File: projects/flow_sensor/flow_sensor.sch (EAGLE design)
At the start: 64 parts, among them IC1 TPS61201, IC5 REG1118

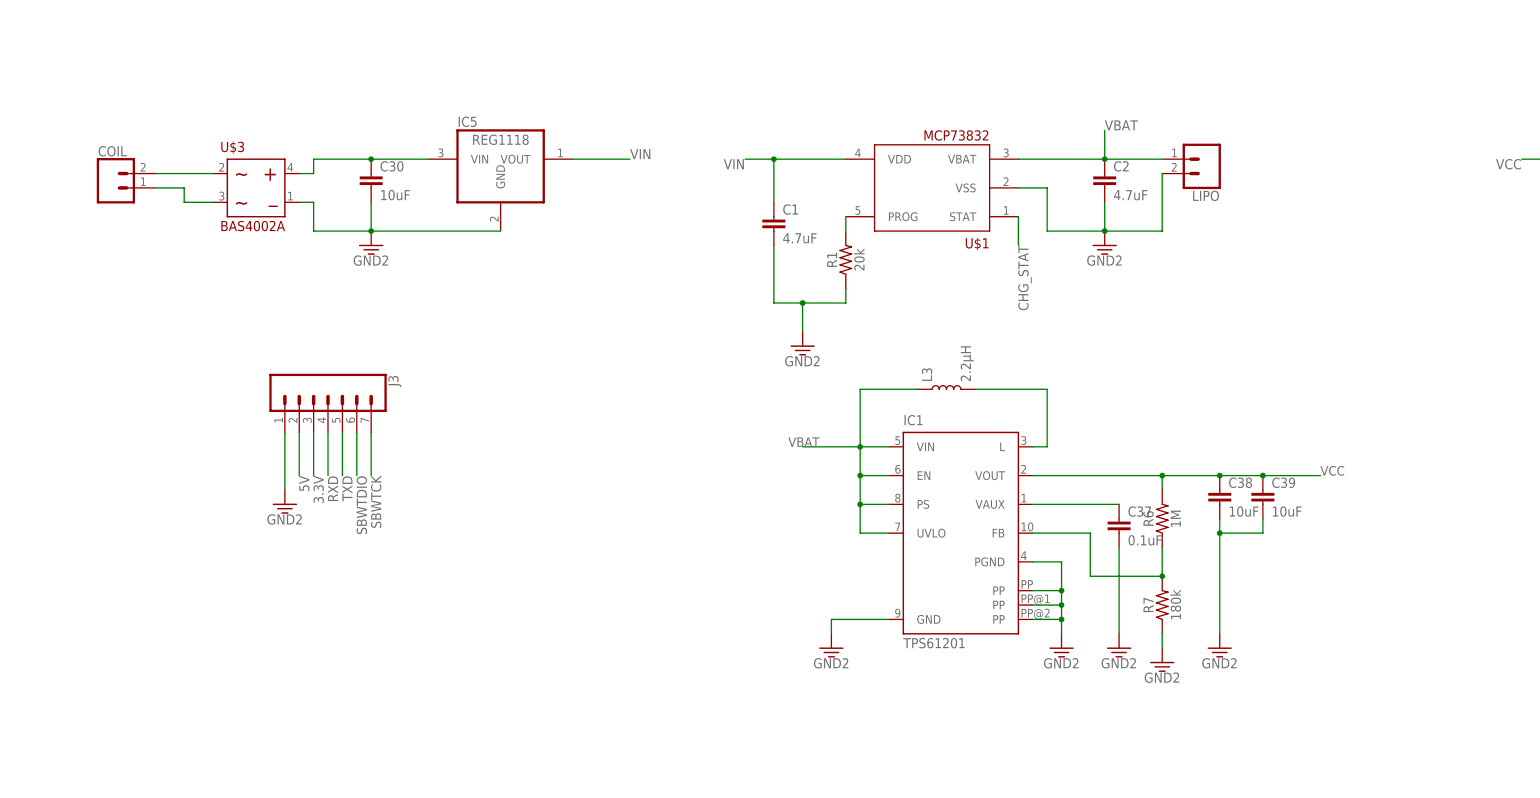
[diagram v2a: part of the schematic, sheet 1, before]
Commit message: Modified power supply to run off of NFC chip supply
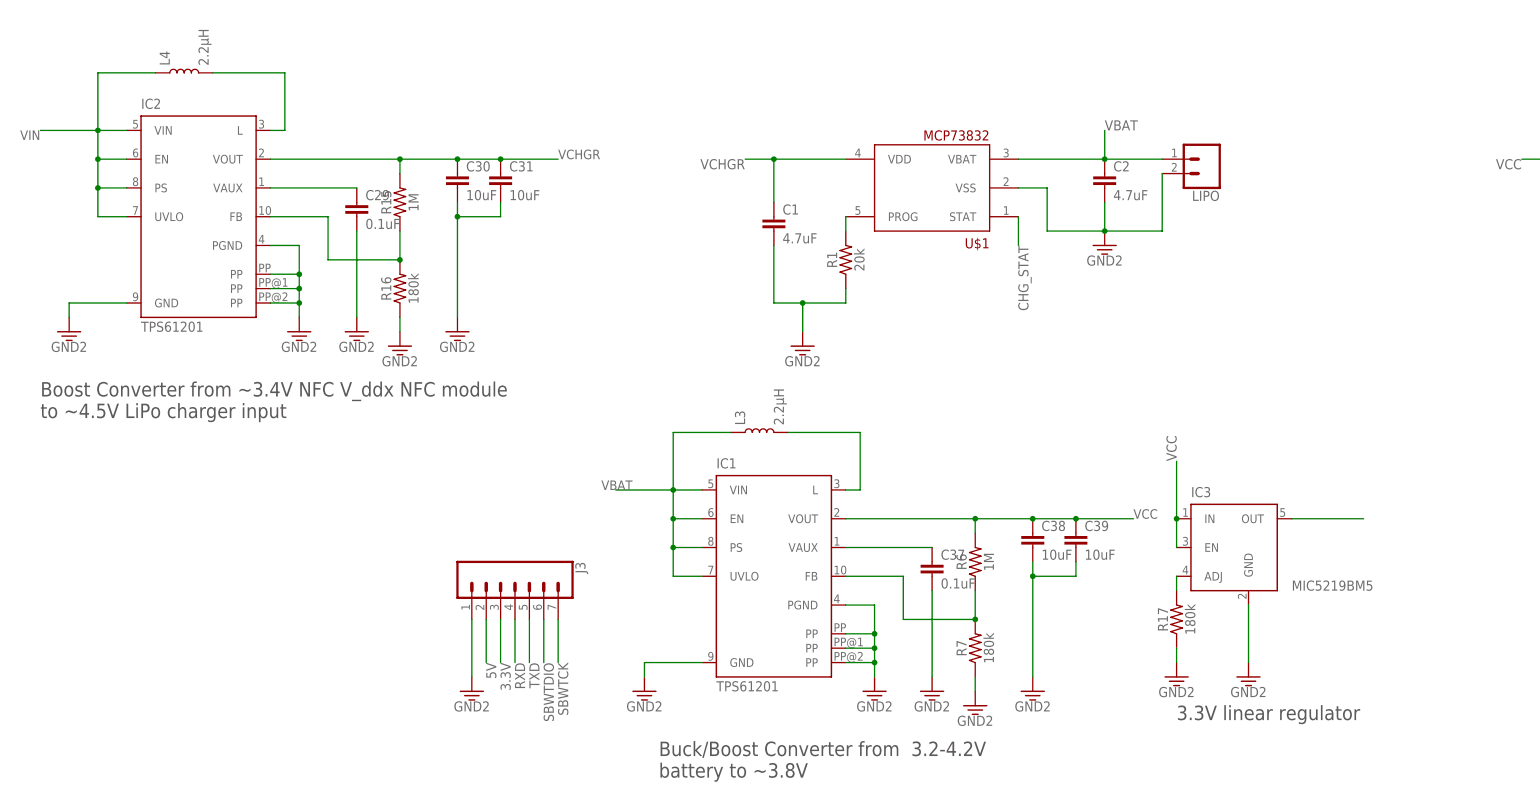
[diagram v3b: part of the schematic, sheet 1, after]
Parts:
- removed COIL: (no value), SparkFun-Connectors:CONN_021X02_NO_SILK
- removed IC5: REG1118, burr-brown:REG1118
- removed U$3: BAS4002A, my_library:BAS4002A
- added C29: 0.1uF, SparkFun-Capacitors:0.1UF-0603-25V-(+80/-20%)
- added C31: 10uF, SparkFun-Capacitors:10UF-0603-6.3V-20%
- added IC2: TPS61201, texas:TPS61201
- added IC3: MIC5219BM5, v-reg-micrel:MIC5219BM5
- added L4: 2.2µH, SparkFun-Coils:INDUCTOR-0805-3.3UH
- added R15: 1M, SparkFun-Resistors:1MOHM-0603-1/4W-5%
- added R16, R17: 180k, SparkFun-Resistors:180OHM-0603-1/10W-1%
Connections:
- removed net POWERCOIL: COIL.2, U$3.~
- removed net POWERCOIL': COIL.1, U$3.~'
- removed net UNREG+: C30.1, IC5.VIN, U$3.+
- new net N$1: IC2.L, L4.2
- new net N$18: C29.1, IC2.VAUX
- new net N$22: IC2.FB, R15.1, R16.2
- new net N$25: IC3.ADJ, R17.2
- new net VCHGR: C1.1, C30.1, C31.1, C5.1, C6.1, IC2.VOUT, R15.2, U$1.VDD, U$2.VIN
- net 3.3V: now also IC3.GND, R17.1
- net GND: now also C29.2, C31.2, IC2.GND, IC2.PGND, IC2.PP, IC2.PP@1, IC2.PP@2, R16.1; no longer IC5.GND, U$3.-
- net N$6: now also IC3.OUT; no longer C7.1, C8.1, R4.1, R5.1, U$2.VDD_I/O, U$2.VDD_X
- net VCC: now also IC3.EN, IC3.IN; no longer C5.1, C6.1, U$2.VIN
- net VIN: now also C7.1, C8.1, IC2.EN, IC2.PS, IC2.UVLO, IC2.VIN, L4.1, R4.1, R5.1, U$2.VDD_I/O, U$2.VDD_X; no longer C1.1, IC5.VOUT, U$1.VDD
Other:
- note added: "3.3V linear regulator"
- note added: "Boost Converter from ~3.4V NFC V_ddx NFC module to ~4.5V LiPo charger input"
- note added: "Buck/Boost Converter from 3.2-4.2V battery to ~3.8V"
- moved on the sheet: C30, C37, C38, C39, IC1, J3, L3, R6, R7

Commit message: Board created, general save dump
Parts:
- added C32, C33: 0.1uF, SparkFun-Capacitors:0.1UF-0603-25V-(+80/-20%)
- added C34, C36: 68.0pF, SparkFun-Capacitors:1.0PF-0603-50V-25%
- added C35, C42: 1.0pF, SparkFun-Capacitors:1.0PF-0603-50V-25%
- added J1, J2: (no value), SparkFun-Connectors:CONN_02
- added R18: 680, SparkFun-Resistors:680OHM-0603-1/10W-5%
- C1: value 4.7uF -> 0.1uF; device SparkFun-Capacitors:4.7UF0603 -> SparkFun-Capacitors:0.1UF-0603-25V-(+80/-20%)
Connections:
- removed net 3.3V: IC3.GND, J3.3, R17.1, U$5.VCC-
- removed net N$6: IC3.OUT
- new net IRQ: U$2.IRQ
- new net N$27: C34.1, C35.1, J1.2
- new net N$30: C38.1, C39.1, IC1.VOUT, IC3.EN, IC3.IN, R6.2
- net ANT: now also J1.1
- net GND: now also C1.1, C32.1, C33.1, C34.2, C35.2, C36.1, C36.2, C42.1, C42.2, IC3.GND, J2.1, J2.2, J3.3, R17.1, R18.1, R18.2, U$5.VCC-; no longer C1.2
- net N$12: now also C15.1, C18.2
- net N$15: now also C15.2, C18.1
- net VCC: now also C1.2, C32.2, C33.2, C5.1, C6.1, IC3.OUT, U$2.VIN; no longer C38.1, C39.1, IC1.VOUT, IC3.EN, IC3.IN, R6.2
- net VCHGR: no longer C1.1, C5.1, C6.1, U$2.VIN
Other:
- moved on the sheet: C1

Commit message: Second data dump.  Board Layout Complete
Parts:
- added C43: 0.1uF, SparkFun-Capacitors:0.1UF-0603-25V-(+80/-20%)
- added C44: 2.2n, SparkFun-Capacitors:1.0UF-0603-16V-10%
- added D1, D2, D3: (no value), SparkFun-LED:LED0603
- added J5: 455-1750-1-ND, SparkFun-Connectors:CONN_03
- added R19, R20: 10k, SparkFun-Resistors:10KOHM-0603-1/10W-1%
- added R21, R22, R23: 680, SparkFun-Resistors:680OHM-0603-1/10W-5%
- added R24: 47k, SparkFun-Resistors:680OHM-0603-1/10W-5%
- added U$6: ADT7320, my_library:ADT7320
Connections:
- removed net CLK: U$2.DATA_CLK, U$9.(UCA0CLK/A5)P1.5
- removed net SIMO: U$2.I/O_7, U$9.(UCA0TXD/UCA0SIMO)P2.0
- removed net SOMI: U$2.I/O_6, U$9.(UCA0RXD/UCA0SOMI)P2.1
- removed net STE: U$9.(UCA0STE/A4)P1.4
- new net 3V3: J3.3
- new net MISO: U$2.I/O_6, U$6.MISO, U$9.(UCB0SCL/UCB0SOMI)P1.7
- new net MOSI: U$2.I/O_7, U$6.MOSI, U$9.(UCB0SDA/UCB0SIMO)P1.6
- new net N$26: R20.2, U$6.CT
- new net N$31: D3.A, R23.1
- new net N$32: D2.A, R22.1
- new net N$33: D1.A, R21.1
- new net N$34: R21.2, U$9.(A8)P4.0
- new net N$35: R22.2, U$9.(A9)P4.1
- new net N$38: R23.2, U$9.(A10)P4.2
- new net N$6: R19.2, U$6.INT
- new net SCLK: U$2.DATA_CLK, U$6.SCLK, U$9.(UCB0CLK)P2.2
- new net TEMP_SS: U$6.CS, U$9.P4.6
- net 5V: now also J5.2
- net CHG_STAT: now also U$9.P3.4
- net COM_EN: now also U$9.P3.5
- net COM_EN2: now also U$9.P3.6
- net COM_SS: now also U$9.P4.5
- net GND: now also C43.2, C44.1, D1.C, D2.C, D3.C, U$6.GND; no longer J3.3
- net IRQ: now also U$9.P3.7
- net N$30: now also J5.1
- net RXD: now also U$9.(UCA0RXD/UCA0SOMI)P2.1
- net SBWTDIO: now also C44.2, R24.1
- net SENSOR_OUT: now also U$9.(A2)P1.2
- net TXD: now also U$9.(UCA0TXD/UCA0SIMO)P2.0
- net VCC: now also C43.1, R19.1, R20.1, R24.2, U$6.VDD
- net VCHGR: now also J5.3
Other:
- moved on the sheet: C19

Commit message: Touched up board V1.0, added labels
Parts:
- IC1, IC2: value TPS61201 -> TPS61200; device texas:TPS61201 -> texas:TPS61200
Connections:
- net COM_EN renamed COMMS_EN
- net COM_EN2 renamed COMMS_EN2
- net COM_SS renamed COMMS_SS
- net IRQ renamed COMMS_IRQ
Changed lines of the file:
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@@
 <part name="C23" library="SparkFun-Capacitors" deviceset="100PF" device="-0603-50V-5%" value="100pF"/>
 <part name="C24" library="SparkFun-Capacitors" deviceset="27PF" device="-0603-50V-5%" value="27pF"/>
-<part name="IC1" library="texas" library_urn="urn:adsk.eagle:library:387" deviceset="TPS6120*" device="" technology="1"/>
+<part name="IC1" library="texas" library_urn="urn:adsk.eagle:library:387" deviceset="TPS6120*" device="" technology="0" value="TPS61200"/>
 <part name="L3" library="SparkFun-Coils" deviceset="INDUCTOR" device="-0805-3.3UH" value="2.2µH"/>
 <part name="R6" library="SparkFun-Resistors" deviceset="1MOHM" device="-0603-1/4W-5%" value="1M"/>
@@
 <part name="R11" library="SparkFun-Resistors" deviceset="1.5KOHM" device="-0603-1/10W-1%" value="1.5k"/>
 <part name="R12" library="SparkFun-Resistors" deviceset="8.2KOHM" device="-0603-1/10W-5%" value="1.5k"/>
-<part name="IC2" library="texas" library_urn="urn:adsk.eagle:library:387" deviceset="TPS6120*" device="" technology="1"/>
+<part name="IC2" library="texas" library_urn="urn:adsk.eagle:library:387" deviceset="TPS6120*" device="" technology="0" value="TPS61200"/>
 <part name="L4" library="SparkFun-Coils" deviceset="INDUCTOR" device="-0805-3.3UH" value="2.2µH"/>
 <part name="R15" library="SparkFun-Resistors" deviceset="1MOHM" device="-0603-1/4W-5%" value="1M"/>
@@
 </segment>
 </net>
-<net name="COM_EN" class="0">
+<net name="COMMS_EN" class="0">
 <segment>
 <pinref part="U$2" gate="G$1" pin="EN"/>
@@
 </segment>
 </net>
-<net name="COM_EN2" class="0">
+<net name="COMMS_EN2" class="0">
 <segment>
 <pinref part="U$2" gate="G$1" pin="EN2"/>
@@
 </segment>
 </net>
-<net name="COM_SS" class="0">
+<net name="COMMS_SS" class="0">
 <segment>
 <pinref part="U$2" gate="G$1" pin="I/O_4"/>
@@
 </segment>
 </net>
-<net name="IRQ" class="0">
+<net name="COMMS_IRQ" class="0">
 <segment>
 <pinref part="U$2" gate="G$1" pin="IRQ"/>

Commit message: starting v2.0
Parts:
- removed R11, R14: 1.5k, SparkFun-Resistors:1.5KOHM-0603-1/10W-1%
- removed R12, R13: 1.5k, SparkFun-Resistors:8.2KOHM-0603-1/10W-5%
- added J4: (no value), SparkFun-Connectors:CONN_021X02_NO_SILK
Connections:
- net GND: no longer R13.2, R14.2
- net N$28: now also J4.2; no longer R11.2, R14.1
- net N$29: now also J4.1; no longer R12.2, R13.1
- net VCC: no longer R11.1, R12.1
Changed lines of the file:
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@@
 <part name="R9" library="SparkFun-Resistors" deviceset="10KOHM" device="-0603-1/10W-1%" value="10k"/>
 <part name="R10" library="SparkFun-Resistors" deviceset="787OHM" device="-0603-1/10W-1%" value="600"/>
-<part name="R13" library="SparkFun-Resistors" deviceset="8.2KOHM" device="-0603-1/10W-5%" value="1.5k"/>
-<part name="R14" library="SparkFun-Resistors" deviceset="1.5KOHM" device="-0603-1/10W-1%" value="1.5k"/>
-<part name="GND24" library="SparkFun-PowerSymbols" deviceset="GND2" device=""/>
 <part name="C28" library="SparkFun-Capacitors" deviceset="4.7UF" device="0603" value="3uF"/>
 <part name="U$4" library="my_library" deviceset="AD8222" device=""/>
@@
 <part name="C41" library="SparkFun-Capacitors" deviceset="4.7UF" device="0603" value="3uF"/>
 <part name="U$5" library="my_library" deviceset="LM321" device=""/>
-<part name="R11" library="SparkFun-Resistors" deviceset="1.5KOHM" device="-0603-1/10W-1%" value="1.5k"/>
-<part name="R12" library="SparkFun-Resistors" deviceset="8.2KOHM" device="-0603-1/10W-5%" value="1.5k"/>
 <part name="IC2" library="texas" library_urn="urn:adsk.eagle:library:387" deviceset="TPS6120*" device="" technology="0" value="TPS61200"/>
 <part name="L4" library="SparkFun-Coils" deviceset="INDUCTOR" device="-0805-3.3UH" value="2.2µH"/>
@@
 <part name="C44" library="SparkFun-Capacitors" deviceset="1.0UF" device="-0603-16V-10%" value="2.2n"/>
 <part name="GND42" library="SparkFun-PowerSymbols" deviceset="GND" device=""/>
+<part name="J4" library="SparkFun-Connectors" deviceset="CONN_02" device="1X02_NO_SILK"/>
 </parts>
 <sheets>
@@
 <instance part="R9" gate="G$1" x="261.62" y="53.34"/>
 <instance part="R10" gate="G$1" x="215.9" y="17.78"/>
-<instance part="R13" gate="G$1" x="180.34" y="55.88"/>
-<instance part="R14" gate="G$1" x="180.34" y="68.58"/>
-<instance part="GND24" gate="G$1" x="190.5" y="63.5" rot="R90"/>
 <instance part="C28" gate="G$1" x="271.78" y="58.42" rot="R90"/>
 <instance part="U$4" gate="G$1" x="215.9" y="43.18"/>
@@
 <instance part="C41" gate="G$1" x="271.78" y="45.72" rot="R270"/>
 <instance part="U$5" gate="G$1" x="304.8" y="50.8"/>
-<instance part="R11" gate="G$1" x="165.1" y="68.58"/>
-<instance part="R12" gate="G$1" x="165.1" y="55.88"/>
 <instance part="IC2" gate="G$1" x="-83.82" y="53.34"/>
 <instance part="L4" gate="G$1" x="-86.36" y="78.74" rot="R90"/>
@@
 <instance part="GND40" gate="1" x="208.28" y="-7.62" rot="R180"/>
 <instance part="J5" gate="J$1" x="55.88" y="17.78"/>
+<instance part="J4" gate="G$1" x="177.8" y="50.8"/>
 </instances>
 <busses>
@@
 <junction x="228.6" y="40.64"/>
 <pinref part="GND21" gate="1" pin="GND"/>
-</segment>
-<segment>
-<pinref part="R13" gate="G$1" pin="2"/>
-<pinref part="R14" gate="G$1" pin="2"/>
-<wire x1="185.42" y1="55.88" x2="185.42" y2="63.5" width="0.1524" layer="91"/>
-<wire x1="185.42" y1="63.5" x2="185.42" y2="68.58" width="0.1524" layer="91"/>
-<wire x1="185.42" y1="63.5" x2="187.96" y2="63.5" width="0.1524" layer="91"/>
-<junction x="185.42" y="63.5"/>
-<pinref part="GND24" gate="G$1" pin="3.3V"/>
 </segment>
 <segment>
@@
 </segment>
 <segment>
-<wire x1="160.02" y1="55.88" x2="160.02" y2="63.5" width="0.1524" layer="91"/>
-<wire x1="160.02" y1="63.5" x2="160.02" y2="68.58" width="0.1524" layer="91"/>
-<wire x1="160.02" y1="63.5" x2="149.86" y2="63.5" width="0.1524" layer="91"/>
-<junction x="160.02" y="63.5"/>
-<label x="149.86" y="63.5" size="1.778" layer="95" rot="R180"/>
-<pinref part="R11" gate="G$1" pin="1"/>
-<pinref part="R12" gate="G$1" pin="1"/>
-</segment>
-<segment>
 <wire x1="309.88" y1="60.96" x2="309.88" y2="66.04" width="0.1524" layer="91"/>
 <pinref part="U$5" gate="G$1" pin="VCC+"/>
@@
 <net name="N$28" class="0">
 <segment>
-<pinref part="R14" gate="G$1" pin="1"/>
-<wire x1="170.18" y1="68.58" x2="172.72" y2="68.58" width="0.1524" layer="91"/>
-<wire x1="172.72" y1="68.58" x2="175.26" y2="68.58" width="0.1524" layer="91"/>
-<wire x1="172.72" y1="68.58" x2="172.72" y2="76.2" width="0.1524" layer="91"/>
-<junction x="172.72" y="68.58"/>
-<wire x1="172.72" y1="76.2" x2="200.66" y2="76.2" width="0.1524" layer="91"/>
-<wire x1="200.66" y1="76.2" x2="200.66" y2="55.88" width="0.1524" layer="91"/>
 <pinref part="U$4" gate="G$1" pin="-IN1"/>
-<wire x1="200.66" y1="55.88" x2="205.74" y2="55.88" width="0.1524" layer="91"/>
-<pinref part="R11" gate="G$1" pin="2"/>
-</segment>
-</net>
-<net name="N$29" class="0">
-<segment>
-<pinref part="R13" gate="G$1" pin="1"/>
-<wire x1="175.26" y1="55.88" x2="172.72" y2="55.88" width="0.1524" layer="91"/>
-<wire x1="172.72" y1="55.88" x2="170.18" y2="55.88" width="0.1524" layer="91"/>
-<wire x1="172.72" y1="48.26" x2="172.72" y2="55.88" width="0.1524" layer="91"/>
-<junction x="172.72" y="55.88"/>
-<pinref part="U$4" gate="G$1" pin="+IN1"/>
-<wire x1="172.72" y1="48.26" x2="205.74" y2="48.26" width="0.1524" layer="91"/>
-<pinref part="R12" gate="G$1" pin="2"/>
+<pinref part="J4" gate="G$1" pin="2"/>
+<wire x1="185.42" y1="53.34" x2="185.42" y2="55.88" width="0.1524" layer="91"/>
+<wire x1="185.42" y1="55.88" x2="205.74" y2="55.88" width="0.1524" layer="91"/>
 </segment>
 </net>
@@
 </segment>
 </net>
+<net name="N$29" class="0">
+<segment>
+<pinref part="U$4" gate="G$1" pin="+IN1"/>
+<pinref part="J4" gate="G$1" pin="1"/>
+<wire x1="205.74" y1="48.26" x2="185.42" y2="48.26" width="0.1524" layer="91"/>
+<wire x1="185.42" y1="48.26" x2="185.42" y2="50.8" width="0.1524" layer="91"/>
+</segment>
+</net>

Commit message: added stuff for board v2
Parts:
- added R11: 180k, SparkFun-Resistors:180OHM-0603-1/10W-1%
- R1: value 20k -> 67k
- R15: value 1M -> 1.6M
- R16: value 180k -> 200k
- R17: value 180k -> 300k
- R21, R22: value 680 -> 47
- R23: value 680 -> 20
- R6: value 1M -> 1.2M
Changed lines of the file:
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@@
 <part name="C2" library="SparkFun-Capacitors" deviceset="4.7UF" device="0603" value="4.7uF"/>
 <part name="LIPO" library="SparkFun-Connectors" deviceset="CONN_02" device="1X02_NO_SILK"/>
-<part name="R1" library="SparkFun-Resistors" deviceset="20KOHM" device="-0603-1/10W-1%" value="20k"/>
+<part name="R1" library="SparkFun-Resistors" deviceset="20KOHM" device="-0603-1/10W-1%" value="67k"/>
 <part name="FRAME3" library="SparkFun-Aesthetics" deviceset="FRAME-A4L" device="">
 <attribute name="CNAME" value="Communications"/>
@@
 <part name="IC1" library="texas" library_urn="urn:adsk.eagle:library:387" deviceset="TPS6120*" device="" technology="0" value="TPS61200"/>
 <part name="L3" library="SparkFun-Coils" deviceset="INDUCTOR" device="-0805-3.3UH" value="2.2µH"/>
-<part name="R6" library="SparkFun-Resistors" deviceset="1MOHM" device="-0603-1/4W-5%" value="1M"/>
+<part name="R6" library="SparkFun-Resistors" deviceset="1MOHM" device="-0603-1/4W-5%" value="1.2M"/>
 <part name="R7" library="SparkFun-Resistors" deviceset="180OHM" device="-0603-1/10W-1%" value="180k"/>
 <part name="FRAME2" library="SparkFun-Aesthetics" deviceset="FRAME-A4L" device="">
@@
 <part name="IC2" library="texas" library_urn="urn:adsk.eagle:library:387" deviceset="TPS6120*" device="" technology="0" value="TPS61200"/>
 <part name="L4" library="SparkFun-Coils" deviceset="INDUCTOR" device="-0805-3.3UH" value="2.2µH"/>
-<part name="R15" library="SparkFun-Resistors" deviceset="1MOHM" device="-0603-1/4W-5%" value="1M"/>
-<part name="R16" library="SparkFun-Resistors" deviceset="180OHM" device="-0603-1/10W-1%" value="180k"/>
+<part name="R15" library="SparkFun-Resistors" deviceset="1MOHM" device="-0603-1/4W-5%" value="1.6M"/>
+<part name="R16" library="SparkFun-Resistors" deviceset="180OHM" device="-0603-1/10W-1%" value="200k"/>
 <part name="C29" library="SparkFun-Capacitors" deviceset="0.1UF" device="-0603-25V-(+80/-20%)" value="0.1uF"/>
 <part name="C30" library="SparkFun-Capacitors" deviceset="10UF" device="-0603-6.3V-20%" value="10uF"/>
 <part name="C31" library="SparkFun-Capacitors" deviceset="10UF" device="-0603-6.3V-20%" value="10uF"/>
 <part name="IC3" library="v-reg-micrel" library_urn="urn:adsk.eagle:library:408" deviceset="MIC5219BM5" device="" package3d_urn="urn:adsk.eagle:package:30272/1"/>
-<part name="R17" library="SparkFun-Resistors" deviceset="180OHM" device="-0603-1/10W-1%" value="180k"/>
+<part name="R17" library="SparkFun-Resistors" deviceset="180OHM" device="-0603-1/10W-1%" value="300k"/>
 <part name="C1" library="SparkFun-Capacitors" deviceset="0.1UF" device="-0603-25V-(+80/-20%)" value="0.1uF"/>
 <part name="C32" library="SparkFun-Capacitors" deviceset="0.1UF" device="-0603-25V-(+80/-20%)" value="0.1uF"/>
@@
 <part name="D2" library="SparkFun-LED" deviceset="LED" device="0603"/>
 <part name="D3" library="SparkFun-LED" deviceset="LED" device="0603"/>
-<part name="R21" library="SparkFun-Resistors" deviceset="680OHM" device="-0603-1/10W-5%" value="680"/>
-<part name="R22" library="SparkFun-Resistors" deviceset="680OHM" device="-0603-1/10W-5%" value="680"/>
-<part name="R23" library="SparkFun-Resistors" deviceset="680OHM" device="-0603-1/10W-5%" value="680"/>
+<part name="R21" library="SparkFun-Resistors" deviceset="680OHM" device="-0603-1/10W-5%" value="47"/>
+<part name="R22" library="SparkFun-Resistors" deviceset="680OHM" device="-0603-1/10W-5%" value="47"/>
+<part name="R23" library="SparkFun-Resistors" deviceset="680OHM" device="-0603-1/10W-5%" value="20"/>
 <part name="GND41" library="SparkFun-PowerSymbols" deviceset="GND" device=""/>
 <part name="J5" library="SparkFun-Connectors" deviceset="CONN_03" device="" value="455-1750-1-ND"/>
@@
 <part name="GND42" library="SparkFun-PowerSymbols" deviceset="GND" device=""/>
 <part name="J4" library="SparkFun-Connectors" deviceset="CONN_02" device="1X02_NO_SILK"/>
+<part name="R11" library="SparkFun-Resistors" deviceset="180OHM" device="-0603-1/10W-1%" value="180k"/>
 </parts>
 <sheets>
@@
 <instance part="J5" gate="J$1" x="55.88" y="17.78"/>
 <instance part="J4" gate="G$1" x="177.8" y="50.8"/>
+<instance part="R11" gate="G$1" x="81.28" y="-17.78" rot="R90"/>
 </instances>
 <busses>
